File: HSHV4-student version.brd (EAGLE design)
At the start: 55 x 57 mm, 17 parts, among them IC1 DS3231, K1 PIN20X2, Q1 MOSFET-NCHANNEL2N7000, Q2 MOSFET-NCHANNEL2N7000

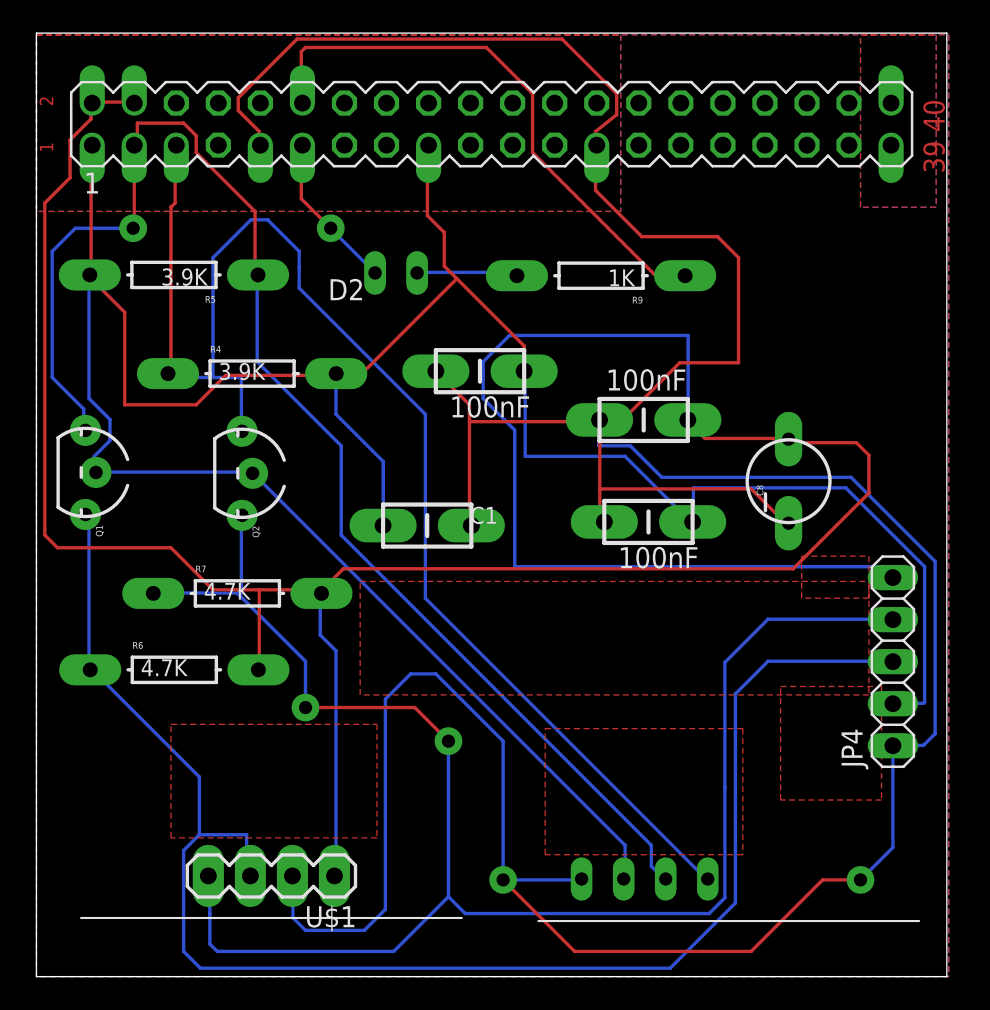
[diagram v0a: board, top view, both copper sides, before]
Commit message: Wire Width 16mil
Wire Width 16mil
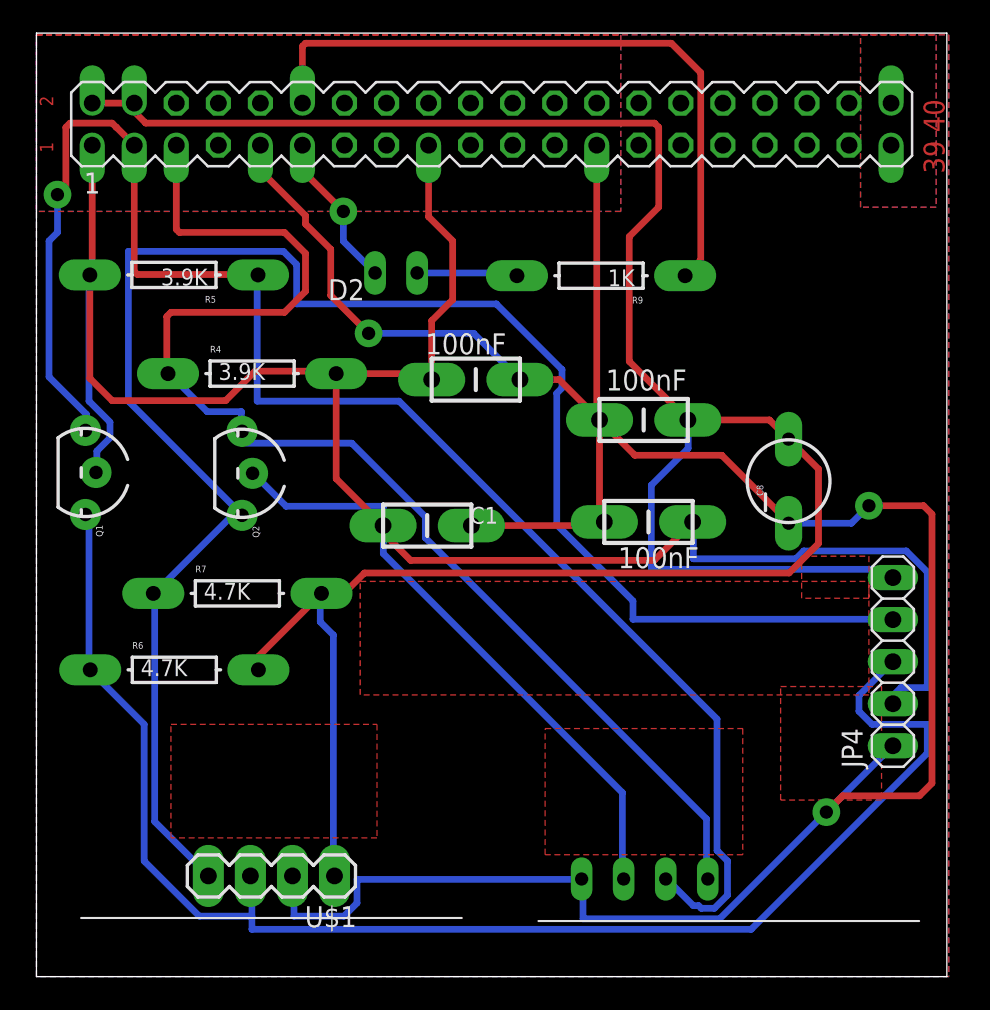
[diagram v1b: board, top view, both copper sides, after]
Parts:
- moved C4 0.57 mm to (26.5, 36.1), turned to 180 degrees
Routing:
- net GND: track 215.2 -> 155.1 mm, vias 2 -> 3
- net +5V: track 174.7 -> 148.3 mm
- net SDA1-3: track 84.5 -> 98.9 mm
- net +3V3: track 167.7 -> 159.7 mm
- net SCL1-5: track 100.6 -> 108.1 mm, vias 2 -> 0
- net GPIO18: track 34.2 -> 41.0 mm
- net SCL1-3: track 84.2 -> 77.5 mm
- net SDA1-5: track 93.4 -> 88.8 mm
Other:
- board text added: "YourName .I"
- board text removed: "YourName"
